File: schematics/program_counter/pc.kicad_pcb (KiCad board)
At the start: 2 copper layers, 100 x 91 mm, 18 parts, among them U1 74HC00, U2 74HC193, U3 74HC193, U4 74HC193, U5 74HC193, U6 74HC245, U7 74HC245

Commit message: silklayer check
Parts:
- moved C3 2.46 mm to (151.3, 88.2)
- moved C6 1.46 mm to (121.2, 60.2)
- moved C7 1.25 mm to (126.2, 44.2)
- moved C2 0.45 mm to (150.8, 104.5)
- moved C5 0.44 mm to (166.9, 44.2)
- moved U5 0.29 mm to (176.5, 67.5)
- moved C8 0.10 mm to (192.5, 115.0)
- moved C4 0.05 mm to (166.9, 59.9)
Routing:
- net VCC: track 85.3 -> 81.3 mm
- net /DL3: track 54.0 -> 55.7 mm
- net /DL2: track 53.8 -> 54.8 mm

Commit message: power change
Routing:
- net GND: track 127.8 -> 190.0 mm
- net VCC: track 81.3 -> 107.1 mm, vias 1 -> 7

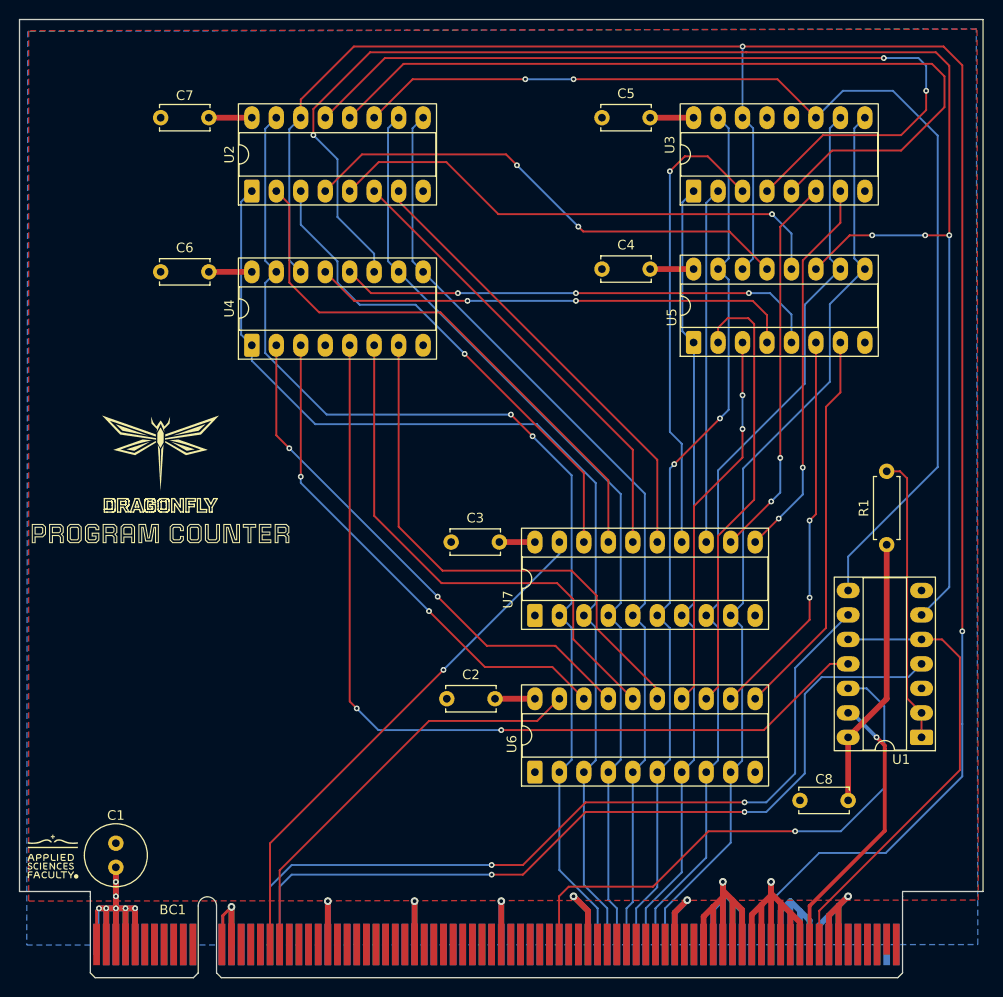
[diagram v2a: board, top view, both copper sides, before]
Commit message: fix: removed in control pins daisy chains
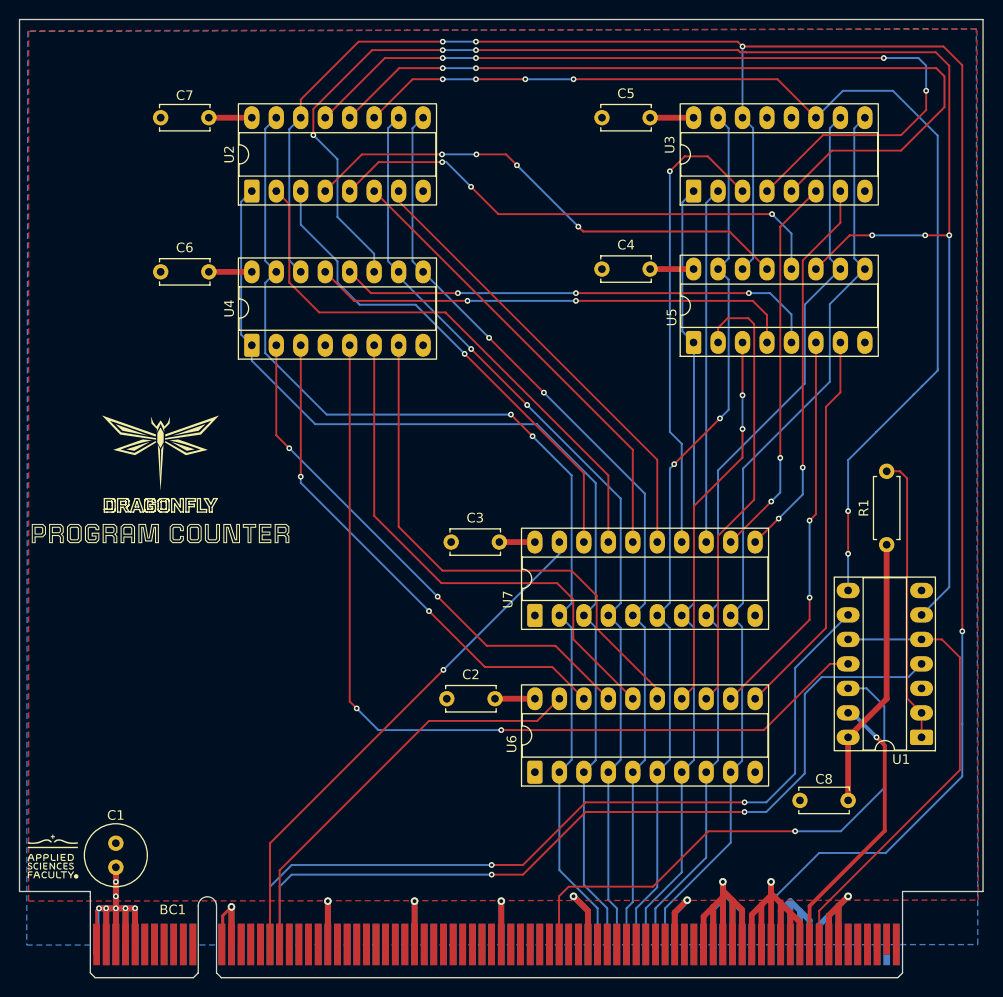
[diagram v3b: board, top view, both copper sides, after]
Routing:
- net /RESET: track 218.2 -> 218.7 mm, vias 2 -> 4
- net Net-(U2-~{CO}): track 87.3 -> 86.9 mm, vias 0 -> 2
- net /Pl: track 162.0 -> 162.2 mm, vias 4 -> 6
- net /Ph: track 115.9 -> 115.8 mm, vias 2 -> 6
- net Net-(U2-~{BO}): track 89.9 -> 90.0 mm, vias 2 -> 4
- net /DATA3: vias 0 -> 2
- net /DATA2: vias 0 -> 2
- net Net-(U2-UP): vias 1 -> 3
- net Net-(U2-DOWN): vias 2 -> 4

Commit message: fix(pc)
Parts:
- moved kibuzzard-6911BE41 78.4 mm to (190.2, 50.2)
- moved C5 66.7 mm to (115.8, 87.0)
- moved U3 66.7 mm to (125.3, 94.6)
- moved C3 43.4 mm to (111.0, 104.5)
- moved U7 43.0 mm to (120.2, 112.1)
- moved C6 37.4 mm to (155.8, 74.4)
- moved U4 37.4 mm to (165.2, 82.0)
- moved U5 32.5 mm to (165.2, 98.0)
- moved C4 32.5 mm to (155.7, 90.4)
- moved U2 29.7 mm to (125.2, 81.0)
- moved C7 29.7 mm to (120.8, 73.4)
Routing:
- net /Pl: track 162.2 -> 47.3 mm, vias 6 -> 1
- net /DATA2: track 98.2 -> 195.9 mm, vias 2 -> 3
- net Net-(U2-~{BO}): track 90.0 -> 22.2 mm, vias 4 -> 0
- net Net-(U2-~{CO}): track 86.9 -> 22.3 mm, vias 2 -> 0
- net /CPu: track 92.8 -> 31.9 mm, vias 2 -> 3
- net /DATA3: track 98.1 -> 147.4 mm, vias 2 -> 5
- net /RESET: track 218.7 -> 181.3 mm
- net /DH4: track 48.7 -> 12.0 mm, vias 1 -> 0
- net /DH1: track 58.4 -> 24.4 mm
- net /DL7: track 40.6 -> 7.51 mm
- net /DL6: track 40.6 -> 7.51 mm, vias 2 -> 0
- net /DL5: track 46.9 -> 15.0 mm
- net /DATA0: track 114.8 -> 146.1 mm, vias 2 -> 3
- net /DL4: track 39.6 -> 8.56 mm, vias 2 -> 0
- net /DATA5: track 82.3 -> 113.0 mm, vias 0 -> 3
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
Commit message: update pc and sp
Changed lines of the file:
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@@
 		(tags "THT DIP DIL PDIP 2.54mm 7.62mm 300mil Socket LongPads")
 		(property "Reference" "U5"
-			(at 2.61 -2.26 90)
+			(at 3.75 -3.47 90)
 			(layer "F.SilkS")
 			(effects
@@
 		(tags "C Disc series Radial pin pitch 5.00mm diameter 5mm width 2.5mm Capacitor")
 		(property "Reference" "C6"
-			(at 2.5 -2.5 0)
+			(at 2.49 2.37 0)
 			(layer "F.SilkS")
 			(effects
@@
 		(tags "THT DIP DIL PDIP 2.54mm 7.62mm 300mil Socket LongPads")
 		(property "Reference" "U7"
-			(at 1.654777 -2.792254 90)
+			(at 3.615735 -2.68 90)
 			(layer "F.SilkS")
 			(effects
@@
 		(tags "THT DIP DIL PDIP 2.54mm 7.62mm 300mil Socket LongPads")
 		(property "Reference" "U6"
-			(at 2.915735 -2.392254 90)
+			(at 4.135735 -3.242254 90)
 			(layer "F.SilkS")
 			(effects
@@
 		(tags "THT DIP DIL PDIP 2.54mm 7.62mm 300mil Socket LongPads")
 		(property "Reference" "U2"
-			(at 3.81 -2.33 90)
+			(at 4.25 -3.22 90)
 			(layer "F.SilkS")
 			(effects
@@
 		(tags "THT DIP DIL PDIP 2.54mm 7.62mm 300mil Socket LongPads")
 		(property "Reference" "U3"
-			(at 4.81 -2.46 90)
+			(at 3.62 -4.26 90)
 			(layer "F.SilkS")
 			(effects
@@
 		(tags "THT DIP DIL PDIP 2.54mm 7.62mm 300mil Socket LongPads")
 		(property "Reference" "U4"
-			(at 3.81 -2.33 90)
-			(layer "F.SilkS")
-			(effects
+			(at 4.25 -2.97 90)
+			(layer "F.SilkS")
+			(effects

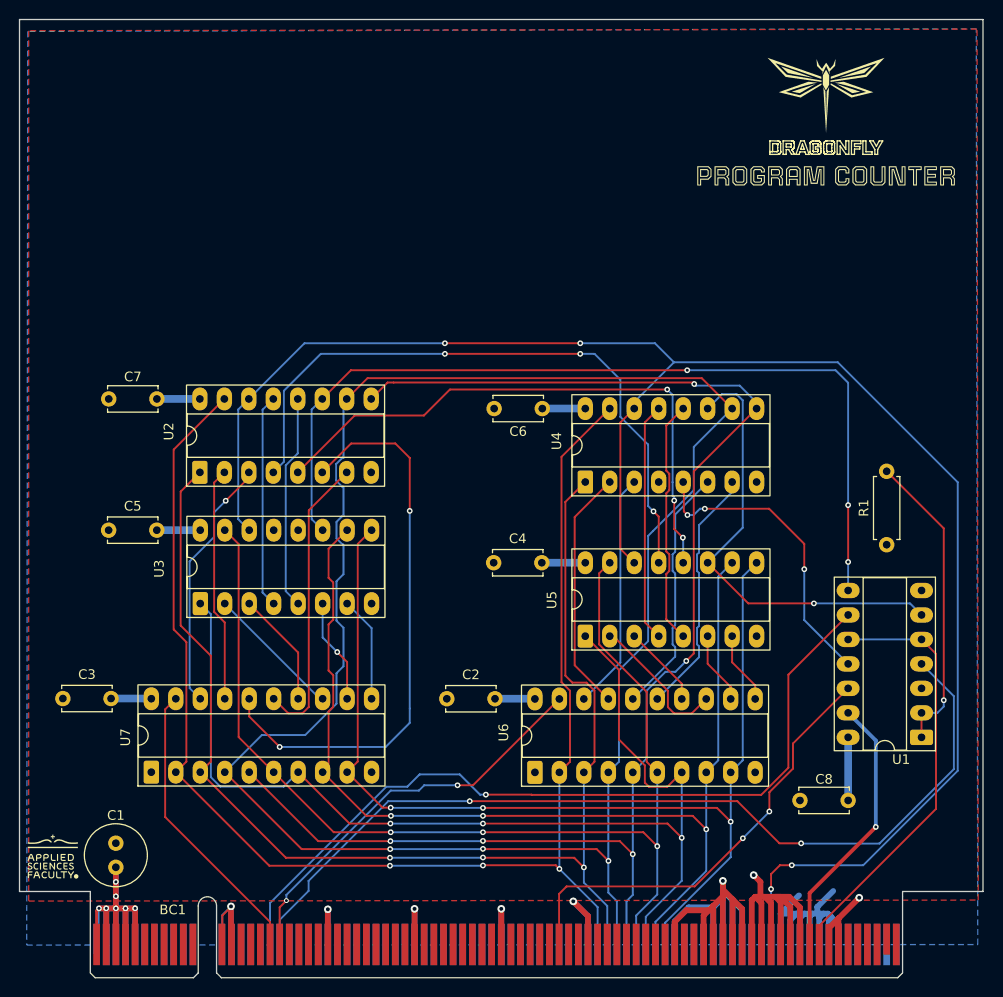
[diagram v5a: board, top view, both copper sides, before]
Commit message: test points sp and pc
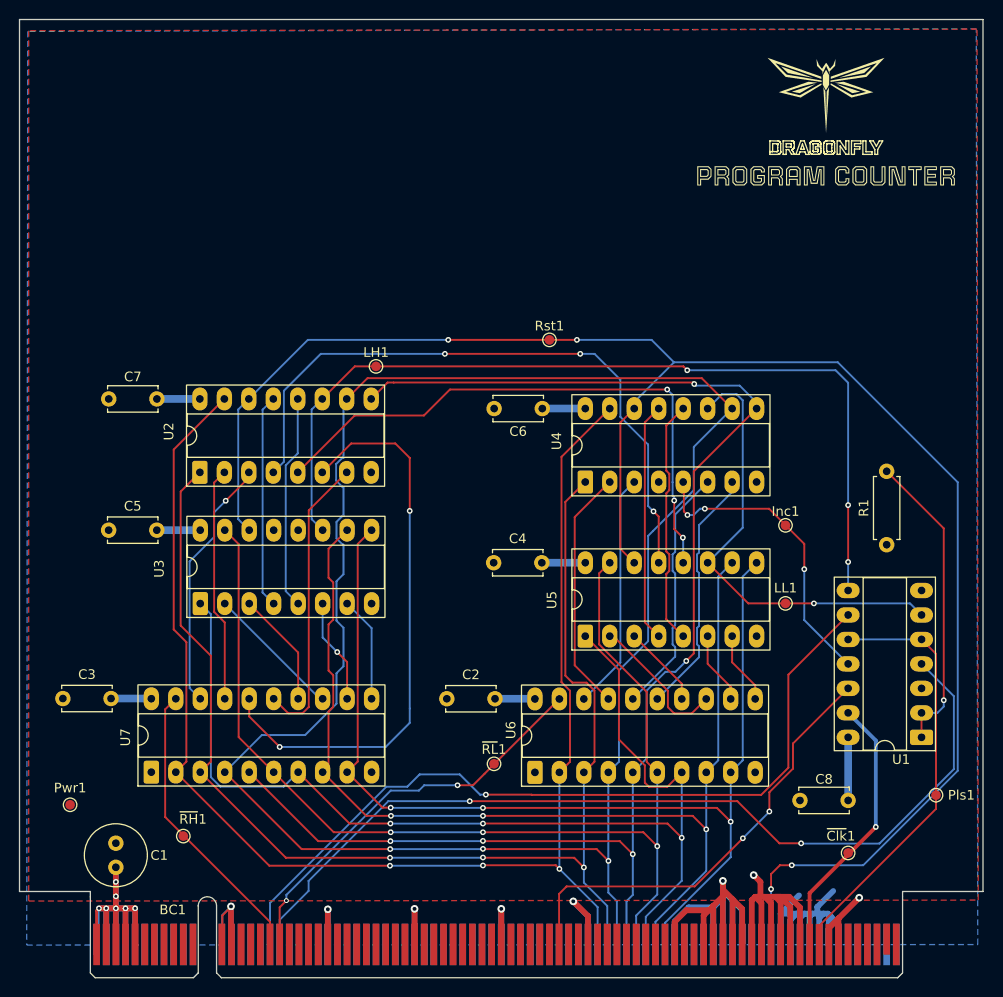
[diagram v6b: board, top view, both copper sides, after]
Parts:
- added Inc1: Increment, TestPoint:TestPoint_Pad_D1.0mm, F.Cu at (186.0, 86.5)
- added LH1: LoadHigh, TestPoint:TestPoint_Pad_D1.0mm, F.Cu at (143.5, 70.0)
- added LL1: LoadLow, TestPoint:TestPoint_Pad_D1.0mm, F.Cu at (186.0, 94.6)
- added Pls1: Pulse, TestPoint:TestPoint_Pad_D1.0mm, F.Cu at (201.6, 114.5)
- added Pwr1: Power, TestPoint:TestPoint_Pad_D1.0mm, F.Cu at (111.8, 115.5)
- added Rst1: Reset, TestPoint:TestPoint_Pad_D1.0mm, F.Cu at (161.5, 67.2)
- added ~{Clk}1: ~{Clock}, TestPoint:TestPoint_Pad_D1.0mm, F.Cu at (192.5, 120.5)
- added ~{RH}1: ~{ReadHigh}, TestPoint:TestPoint_Pad_D1.0mm, F.Cu at (123.5, 118.8)
- added ~{RL}1: ~{ReadLow}, TestPoint:TestPoint_Pad_D1.0mm, F.Cu at (155.8, 111.2)

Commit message: done
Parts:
- added kibuzzard-691DE17B: G***, kibuzzard-691DE17B, F.Cu at (203.5, 71.0)
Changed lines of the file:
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@@
+		(embedded_fonts no)
+	)
+	(footprint "kibuzzard-691DE17B"
+		(layer "F.Cu")
+		(at 203.5 71 90)
+		(descr "Generated with KiBuzzard")
+		(tags "kb_params=eyJBbGlnbm1lbnRDaG9pY2UiOiAiQ2VudGVyIiwgIkNhcExlZnRDaG9pY2UiOiAiIiwgIkNhcFJpZ2h0Q2hvaWNlIjogIi8iLCAiRm9udENvbWJvQm94IjogIlRvdXJuZXktUmVndWxhciIsICJIZWlnaHRDdHJsIjogMi4wLCAiTGF5ZXJDb21ib0JveCI6ICJGLlNpbGtTIiwgIkxpbmVTcGFjaW5nQ3RybCI6IDEuNSwgIk11bHRpTGluZVRleHQiOiAiVUNVIEFQUFMuXG4iLCAiUGFkZGluZ0JvdHRvbUN0cmwiOiA1LjAsICJQYWRkaW5nTGVmdEN0cmwiOiA1LjAsICJQYWRkaW5nUmlnaHRDdHJsIjogNS4wLCAiUGFkZGluZ1RvcEN0cmwiOiA1LjAsICJXaWR0aEN0cmwiOiAyLjAsICJhZHZhbmNlZENoZWNrYm94IjogdHJ1ZSwgImlubGluZUZvcm1hdFRleHRib3giOiB0cnVlLCAibGluZW92ZXJTdHlsZUNob2ljZSI6ICJTcXVhcmUiLCAibGluZW92ZXJUaGlja25lc3NDdHJsIjogMX0=")
+		(property "Reference" "kibuzzard-691DE17B"
+			(at 0 -4.048 90)
+			(layer "F.SilkS")
+			(hide yes)
+			(effects
+				(font
+					(size 0.001 0.001)
+					(thickness 0.15)
+				)
+			)
+		)
+		(property "Value" "G***"
+			(at 0 4.048 90)
+			(layer "F.SilkS")
+			(hide yes)
+			(effects
+				(font
+					(size 0.001 0.001)
+					(thickness 0.15)
+				)
+			)
+		)
+		(property "Datasheet" ""
+			(at 0 0 90)
+			(layer "F.Fab")
+			(hide yes)
+			(effects
+				(font
+					(size 1.27 1.27)
+					(thickness 0.15)
+				)
+			)
+		)
+		(property "Description" ""
+			(at 0 0 90)
+			(layer "F.Fab")
+			(hide yes)
+			(effects
+				(font
+					(size 1.27 1.27)
+					(thickness 0.15)
+				)
+			)
+		)
+		(attr board_only exclude_from_pos_files exclude_from_bom)
+		(fp_poly
+			(pts
+				(xy 6.606429 1) (xy 6.606429 0.58) (xy 7.055 0.58) (xy 7.055 1) (xy 6.722143 1) (xy 6.722143 0.885714)
+				(xy 6.940714 0.885714) (xy 6.940714 0.692857) (xy 6.722143 0.692857) (xy 6.722143 0.885714) (xy 6.722143 1)
+				(xy 6.606429 1)
+			)
+			(stroke
+				(width 0)
+				(type solid)
+			)
+			(fill yes)
+			(layer "F.SilkS")
+		)
+		(fp_poly
+			(pts
+				(xy 3.246429 0.105714) (xy 3.246429 -0.708571) (xy 4.002143 -0.708571) (xy 4.146429 -0.565714) (xy 4.146429 -0.064286)
+				(xy 3.975 0.105714) (xy 3.357857 0.105714) (xy 3.357857 -0.001429) (xy 3.916429 -0.001429) (xy 4.032143 -0.115714)
+				(xy 4.032143 -0.508571) (xy 3.945 -0.595714) (xy 3.357857 -0.595714) (xy 3.357857 -0.001429) (xy 3.357857 0.105714)
+				(xy 3.246429 0.105714)
+			)
+			(stroke
+				(width 0)
+				(type solid)
+			)
+			(fill yes)
+			(layer "F.SilkS")
+		)
+		(fp_poly
+			(pts
+				(xy 1.449286 0.105714) (xy 1.449286 -0.708571) (xy 2.205 -0.708571) (xy 2.349286 -0.565714) (xy 2.349286 -0.064286)
+				(xy 2.177857 0.105714) (xy 1.560714 0.105714) (xy 1.560714 -0.001429) (xy 2.119286 -0.001429) (xy 2.235 -0.115714)
+				(xy 2.235 -0.508571) (xy 2.147857 -0.595714) (xy 1.560714 -0.595714) (xy 1.560714 -0.001429) (xy 1.560714 0.105714)
+				(xy 1.449286 0.105714)
+			)
+			(stroke
+				(width 0)
+				(type solid)
+			)
+			(fill yes)
+			(layer "F.SilkS")
+		)
+		(fp_poly
+			(pts
+				(xy -0.400714 0.12) (xy -0.400714 -0.568571) (xy -0.256429 -0.712857) (xy 0.376429 -0.712857) (xy 0.520714 -0.568571)
+				(xy 0.520714 0.12) (xy -0.295 0.12) (xy -0.295 0.008571) (xy 0.410714 0.008571) (xy 0.410714 -0.508571)
+				(xy 0.323571 -0.595714) (xy -0.207857 -0.595714) (xy -0.295 -0.508571) (xy -0.295 0.008571) (xy -0.295 0.12)
+				(xy -0.400714 0.12)
+			)
+			(stroke
+				(width 0)
+				(type solid)
+			)
+			(fill yes)
+			(layer "F.SilkS")
+		)
+		(fp_poly
+			(pts
+				(xy 2.953571 1) (xy 2.953571 -1) (xy 4.140714 -1) (xy 4.435 -0.705714) (xy 4.435 0.081429) (xy 4.113571 0.402857)
+				(xy 3.357857 0.402857) (xy 3.357857 1) (xy 3.062143 1) (xy 3.062143 0.902857) (xy 3.246429 0.902857)
+				(xy 3.246429 0.288571) (xy 4.065 0.288571) (xy 4.329286 0.022857) (xy 4.329286 -0.654286) (xy 4.090714 -0.892857)
+				(xy 3.062143 -0.892857) (xy 3.062143 0.902857) (xy 3.062143 1) (xy 2.953571 1)
+			)
+			(stroke
+				(width 0)
+				(type solid)
+			)
+			(fill yes)
+			(layer "F.SilkS")
+		)
+		(fp_poly
+			(pts
+				(xy 1.156429 1) (xy 1.156429 -1) (xy 2.343571 -1) (xy 2.637857 -0.705714) (xy 2.637857 0.081429)
+				(xy 2.316429 0.402857) (xy 1.560714 0.402857) (xy 1.560714 1) (xy 1.265 1) (xy 1.265 0.902857) (xy 1.449286 0.902857)
+				(xy 1.449286 0.288571) (xy 2.267857 0.288571) (xy 2.532143 0.022857) (xy 2.532143 -0.654286) (xy 2.293571 -0.892857)
+				(xy 1.265 -0.892857) (xy 1.265 0.902857) (xy 1.265 1) (xy 1.156429 1)
+			)
+			(stroke
+				(width 0)
+				(type solid)
+			)
+			(fill yes)
+			(layer "F.SilkS")
+		)
+		(fp_poly
+			(pts
+				(xy -0.697857 1) (xy -0.697857 -0.705714) (xy -0.403571 -1) (xy 0.519286 -1) (xy 0.813571 -0.705714)
+				(xy 0.813571 1) (xy 0.410714 1) (xy 0.410714 0.411429) (xy -0.295 0.411429) (xy -0.295 1) (xy -0.583571 1)
+				(xy -0.583571 0.881429) (xy -0.400714 0.881429) (xy -0.400714 0.304286) (xy 0.520714 0.304286) (xy 0.520714 0.881429)
+				(xy 0.705 0.881429) (xy 0.705 -0.657143) (xy 0.465 -0.895714) (xy -0.345 -0.895714) (xy -0.583571 -0.657143)
+				(xy -0.583571 0.881429) (xy -0.583571 1) (xy -0.697857 1)
+			)
+			(stroke
+				(width 0)
+				(type solid)
+			)
+			(fill yes)
+			(layer "F.SilkS")
+		)
+		(fp_poly
+			(pts
+				(xy -3.086429 1) (xy -3.380714 0.705714) (xy -3.380714 -1) (xy -2.976429 -1) (xy -2.976429 0.508571)
+				(xy -2.889286 0.595714) (xy -2.303571 0.595714) (xy -2.216429 0.508571) (xy -2.216429 -1) (xy -1.812143 -1)
+				(xy -1.812143 0.705714) (xy -2.106429 1) (xy -3.030714 1) (xy -3.030714 0.89) (xy -2.160714 0.89)
+				(xy -1.922143 0.652857) (xy -1.922143 -0.892857) (xy -2.105 -0.892857) (xy -2.105 0.564286) (xy -2.250714 0.705714)
+				(xy -2.940714 0.705714) (xy -3.086429 0.564286) (xy -3.086429 -0.892857) (xy -3.270714 -0.892857)
+				(xy -3.270714 0.652857) (xy -3.030714 0.89) (xy -3.030714 1) (xy -3.086429 1)
+			)
+			(stroke
+				(width 0)
+				(type solid)
+			)
+			(fill yes)
+			(layer "F.SilkS")
+		)
+		(fp_poly
+			(pts
+				(xy -6.760714 1) (xy -7.055 0.705714) (xy -7.055 -1) (xy -6.650714 -1) (xy -6.650714 0.508571) (xy -6.563571 0.595714)
+				(xy -5.977857 0.595714) (xy -5.890714 0.508571) (xy -5.890714 -1) (xy -5.486429 -1) (xy -5.486429 0.705714)
+				(xy -5.780714 1) (xy -6.705 1) (xy -6.705 0.89) (xy -5.835 0.89) (xy -5.596429 0.652857) (xy -5.596429 -0.892857)
+				(xy -5.779286 -0.892857) (xy -5.779286 0.564286) (xy -5.925 0.705714) (xy -6.615 0.705714) (xy -6.760714 0.564286)
+				(xy -6.760714 -0.892857) (xy -6.945 -0.892857) (xy -6.945 0.652857) (xy -6.705 0.89) (xy -6.705 1)
+				(xy -6.760714 1)
+			)
+			(stroke
+				(width 0)
+				(type solid)
+			)
+			(fill yes)
+			(layer "F.SilkS")
+		)
+		(fp_poly
+			(pts
+				(xy -4.877857 1) (xy -5.172143 0.705714) (xy -5.172143 -0.705714) (xy -4.877857 -1) (xy -3.990714 -1)
+				(xy -3.695 -0.705714) (xy -3.695 -0.245714) (xy -4.099286 -0.245714) (xy -4.099286 -0.508571) (xy -4.186429 -0.595714)
+				(xy -4.680714 -0.595714) (xy -4.767857 -0.508571) (xy -4.767857 0.508571) (xy -4.680714 0.595714)
+				(xy -4.186429 0.595714) (xy -4.099286 0.508571) (xy -4.099286 0.245714) (xy -3.695 0.245714) (xy -3.695 0.705714)
+				(xy -3.990714 1) (xy -4.823571 1) (xy -4.823571 0.888571) (xy -4.043571 0.888571) (xy -3.805 0.65)
+				(xy -3.805 0.344286) (xy -3.987857 0.344286) (xy -3.987857 0.561429) (xy -4.133571 0.705714) (xy -4.733571 0.705714)
+				(xy -4.879286 0.561429) (xy -4.879286 -0.565714) (xy -4.733571 -0.708571) (xy -4.133571 -0.708571)
+				(xy -3.987857 -0.565714) (xy -3.987857 -0.348571) (xy -3.805 -0.348571) (xy -3.805 -0.654286) (xy -4.043571 -0.892857)
+				(xy -4.823571 -0.892857) (xy -5.062143 -0.654286) (xy -5.062143 0.65) (xy -4.823571 0.888571) (xy -4.823571 1)
+				(xy -4.877857 1)
+			)
+			(stroke
+				(width 0)
+				(type solid)
+			)
+			(fill yes)
+			(layer "F.SilkS")
+		)
+		(fp_poly
+			(pts
+				(xy 5.030714 1) (xy 4.736429 0.705714) (xy 4.736429 0.345714) (xy 5.140714 0.345714) (xy 5.140714 0.508571)
+				(xy 5.227857 0.595714) (xy 5.776429 0.595714) (xy 5.863571 0.508571) (xy 5.863571 0.288571) (xy 5.776429 0.201429)
+				(xy 5.039286 0.201429) (xy 4.745 -0.092857) (xy 4.745 -0.705714) (xy 5.039286 -1) (xy 5.946429 -1)
+				(xy 6.240714 -0.705714) (xy 6.240714 -0.345714) (xy 5.836429 -0.345714) (xy 5.836429 -0.508571)
+				(xy 5.749286 -0.595714) (xy 5.236429 -0.595714) (xy 5.147857 -0.508571) (xy 5.147857 -0.29) (xy 5.236429 -0.202857)
+				(xy 5.973571 -0.202857) (xy 6.267857 0.091429) (xy 6.267857 0.705714) (xy 5.973571 1) (xy 5.082143 1)
+				(xy 5.082143 0.89) (xy 5.915 0.89) (xy 6.153571 0.651429) (xy 6.153571 0.131429) (xy 5.929286 -0.094286)
+				(xy 5.185 -0.094286) (xy 5.039286 -0.238571) (xy 5.039286 -0.562857) (xy 5.183571 -0.705714) (xy 5.807857 -0.705714)
+				(xy 5.946429 -0.57) (xy 5.946429 -0.447143) (xy 6.129286 -0.447143) (xy 6.129286 -0.658571) (xy 5.897857 -0.89)
+				(xy 5.093571 -0.89) (xy 4.855 -0.651429) (xy 4.855 -0.151429) (xy 5.096429 0.091429) (xy 5.839286 0.091429)
+				(xy 5.969286 0.217143) (xy 5.969286 0.562857) (xy 5.825 0.707143) (xy 5.172143 0.707143) (xy 5.035 0.57)
+				(xy 5.035 0.447143) (xy 4.850714 0.447143) (xy 4.850714 0.658571) (xy 5.082143 0.89) (xy 5.082143 1)
+				(xy 5.030714 1)
+			)
+			(stroke
+				(width 0)
+				(type solid)
+			)
+			(fill yes)
+			(layer "F.SilkS")
+		)
 		(embedded_fonts no)
 	)
